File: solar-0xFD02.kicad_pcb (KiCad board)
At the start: 2 copper layers, 25.4 x 25.4 mm, 34 parts, among them J1 Solar, J2 BAT+, J3 BAT-, J4 ESP32, Q1 P-Chan, Q2 P-Chan, U1 CN3801, U2 NCP302HSN30

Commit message: Improvements
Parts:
- moved C10 15.2 mm to (143.0, 75.8), turned to 90 degrees
- moved Q2 8.19 mm to (132.3, 83.8)
- moved D5 8.14 mm to (132.7, 91.2), turned to 180 degrees
- moved R6 2.30 mm to (132.8, 93.6)
- moved R9 0.06 mm to (139.0, 74.2)
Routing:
- net /BAT+: track 42.9 -> 48.7 mm
- net /ESP-LOAD: track 37.2 -> 33.2 mm
- net /GND: track 134.9 -> 131.7 mm
- net Net-(D5-Pad1): track 2.71 -> 4.67 mm
- net /ADC: track 14.8 -> 16.2 mm
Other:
- board text added: ".01"

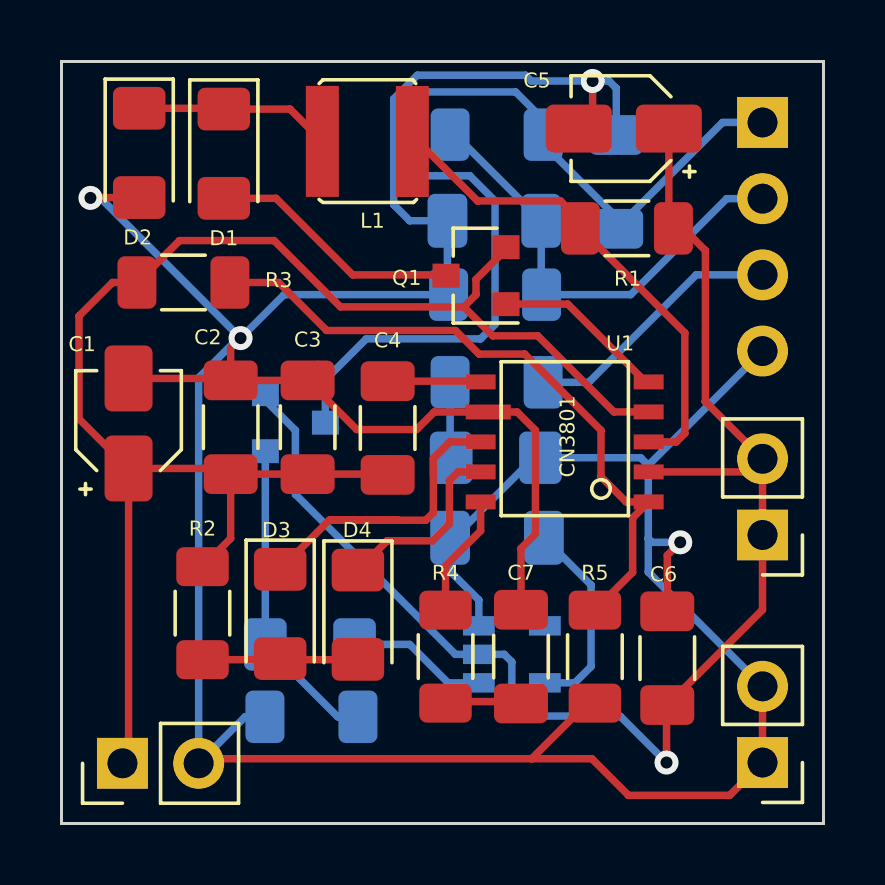
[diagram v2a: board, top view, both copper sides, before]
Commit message: Made some footprints larger for easier soldering experience.
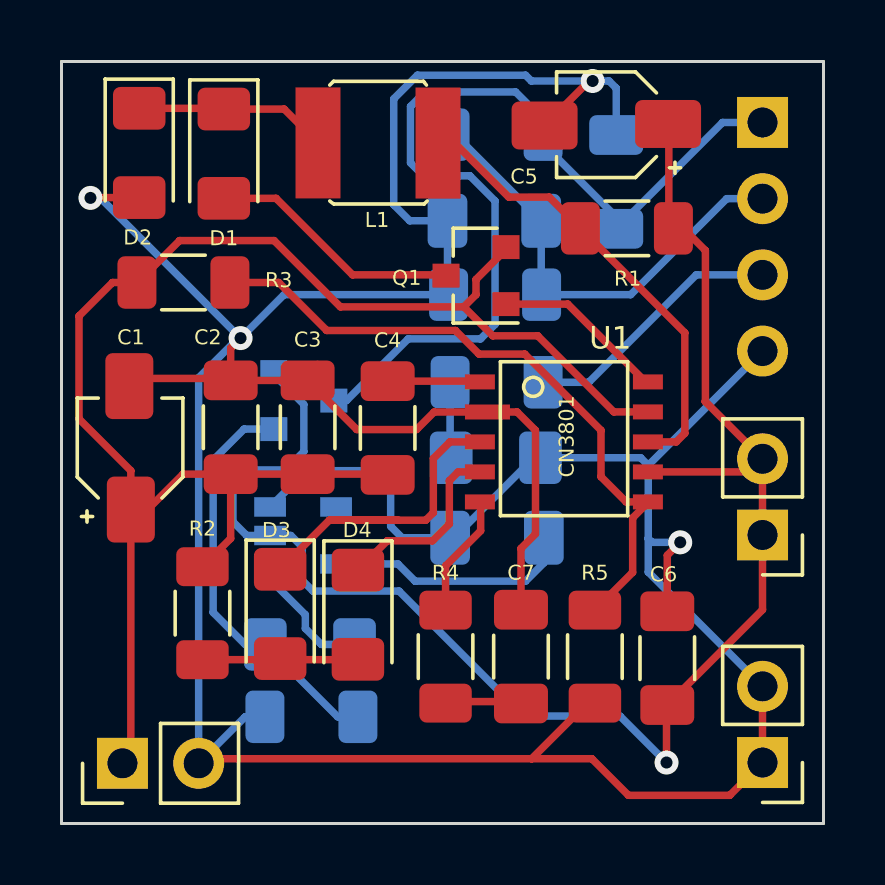
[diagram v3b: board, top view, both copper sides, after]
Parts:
- C1, C5: footprint Capacitor_SMD:CP_Elec_3x5.4 -> 0xFD:CP_Elec_3x6.4
- Q1: value P-Chan -> DMP1045U-7
- Q2: value P-Chan -> SSM3J332RLF
- R1: value Rcs -> 0.24
- R3: value 100k -> 300k
- R5: value Rx -> 100k
- moved U2 8.01 mm to (132.5, 87.6)
- moved C1 0.92 mm to (126.7, 84.7)
- moved Q2 0.79 mm to (132.5, 83.1)
- moved C5 0.50 mm to (142.7, 73.9)
- moved L1 0.36 mm to (135.6, 72.6)
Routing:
- net /GND: track 131.7 -> 137.0 mm
- net /BAT+: track 48.7 -> 53.6 mm
- net /LVCO: track 10.5 -> 13.8 mm
- net /Cd: track 6.71 -> 8.26 mm
- net /ESP-LOAD: track 33.2 -> 31.8 mm
- net /CSP: track 16.7 -> 15.5 mm
- net /SOL+: track 52.9 -> 53.9 mm

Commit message: Fixed zener diode pad
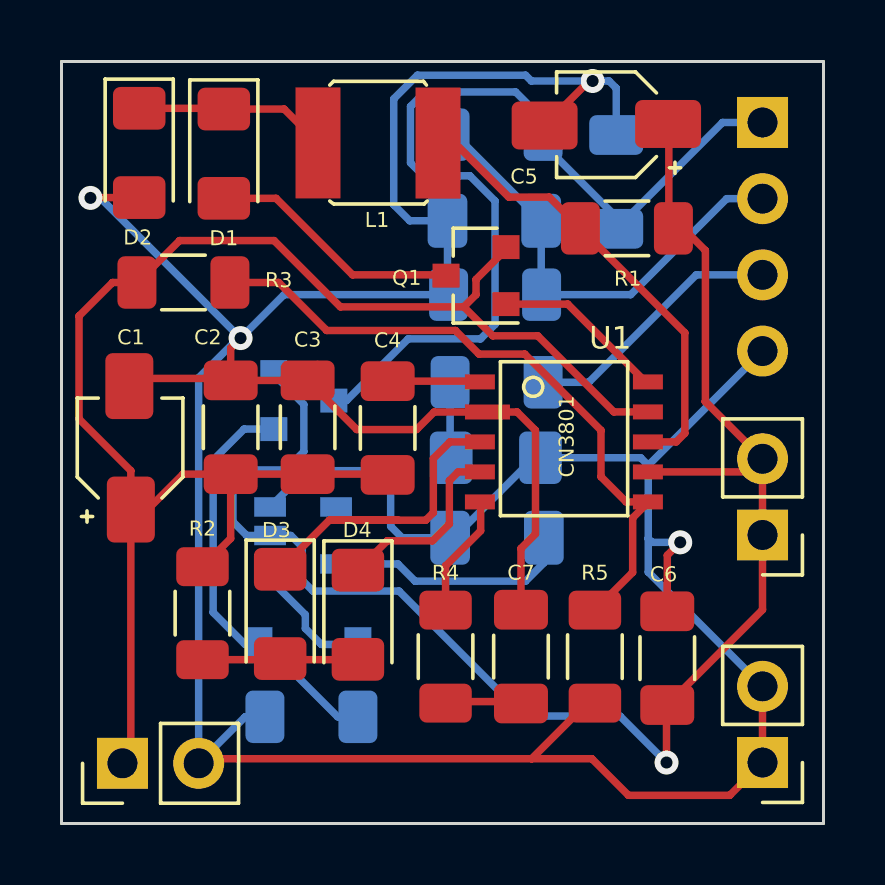
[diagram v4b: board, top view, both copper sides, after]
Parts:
- D5: footprint Diode_SMD:D_1206_3216Metric_Pad1.42x1.75mm_HandSolder -> Diode_SMD:D_SOD-123
- moved D5 0.06 mm to (132.7, 91.2)
